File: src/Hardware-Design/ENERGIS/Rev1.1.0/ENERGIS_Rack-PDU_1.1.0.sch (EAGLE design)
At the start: 423 parts, among them IC1 MP2315GJ-Z, IC10 HLW8032, IC11 HLW8032, IC12 HLW8032, IC13 MP150GJ, IC14 HLW8032, IC15 RP2040, IC16 HLW8032, IC17 MCP6001RT-I/OT, IC18 W25Q128JVPIQ, IC19 CAT24C256HU4IGT3, IC2 MP2315GJ-Z, IC20 W5500, IC21 MIC5504-3.3YM5, IC22 MCP6001RT-I/OT, IC3 ULN2803AFWG, IC4 MCP23017T-E/ML, IC5 MP150GJ, IC6 HLW8032, IC7 HLW8032, IC8 HLW8032, IC9 SN74HC151PWR, J10 0R 1%, J2 JP, J7 JP, J8 0R 1%, J9 0R 1%, K1 G2RL-1A-E DC12, K2 G2RL-1A-E DC12, K3 G2RL-1A-E DC12, K4 G2RL-1A-E DC12, K5 G2RL-1A-E DC12, K6 G2RL-1A-E DC12, K7 G2RL-1A-E DC12, K8 G2RL-1A-E DC12, P12ON Green, P3ON Green, P5ON Green, SW3 TP, X1 ABM8-272-T3 12MHz, X2 25MHz

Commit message: add pcap tests. Small fixes
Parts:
- removed FB-NI1, FB-NI2, VNI1, VNI2: TP, ds_passive:TP
- removed GDGC: (no value), ds_con:CON-1X4
- added ADC12, FB1, FB2, VCC, VCC2: TP-ROUND, ds_passive:TP-ROUND
- added GDRC: (no value), ds_con:CON-1X4
- 12VDC, 5V-NI1, 5V-NI2, L-REC1, L-REC2, REL0, REL1, REL2, REL3, REL4, REL5, REL6, REL7, RX0, RX1, SCL0, SCL1, SDA0, SDA1: value TP -> TP-ROUND; device ds_passive:TP -> ds_passive:TP-ROUND
- R17, R18, R19, R20, R21, R22, R23, R24: value 330R 1% 1W -> 0R 1%; device ds_resistor:330R-1%-2512 -> ds_resistor:0R2512
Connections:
- net +12V_MEA: now also ADC12.P$1
- net FB1: now also FB1.P$1; no longer FB-NI1.P$1
- net FB2: now also FB2.P$1; no longer FB-NI2.P$1
- net GND: now also GDRC.P$4; no longer GDGC.P$4
- net RUN: now also GDRC.P$2; no longer GDGC.P$2
- net SWCLK: now also GDRC.P$1; no longer GDGC.P$1
- net SWDIO: now also GDRC.P$3; no longer GDGC.P$3
- net VNI1: now also VCC.P$1; no longer VNI1.P$1
- net VNI2: now also VCC2.P$1; no longer VNI2.P$1
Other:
- note added: "12VDC"
- note added: "230VAC"
- note added: "5V NON-ISOLATED"
- note added: "DEBUG CONNECTOR"
- note added: "Design Note — 12 V supply (Mean Well IRM-10 series), universal 110 V/230 V AC This schematic uses the Mean Well IRM-10 encapsulated AC-DC module (e.g., IRM-10-12) to produce 12 VDC. The IRM-10 series is specified for a wide input range of 85–305 VAC (47–440 Hz) and 120–430 VDC, meaning it operates from both ~115 VAC and ~230 VAC mains with no selector or changes to the circuit. Safety approvals (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"
- note added: "Design Note — 5 V / 200 mA non-isolated supply (MP150), universal 110 V/230 V AC This design uses MPS MP150 in high-side buck to generate 5 V/200 mA directly from rectified mains. MP150 integrates a 500 V MOSFET (Drain-to-Source rating 500 V), covering the ~325 VDC peak from 230 VAC and ~155 VDC from 115 VAC, so the circuit from 85–265 VAC (“universal input”)."
- note added: "ENABLE/DISABLE"
- note added: "FAN CONNECTOR"
- note added: "MCU"
- note added: "PERIPHERALS"
- note added: "USB-C 5VDC"
- note removed: "5V AC-MEASUREMENT"
- note removed: "DEBUG"
- note removed: "FAN"
- note removed: "Rev 1.0.1"

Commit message: adapt design to NextPCB dru
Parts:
- removed CS0, MISO0, MOSI0, SCLK0: TP, ds_passive:TP
- added CS, MI, MO, SC: TP-ROUND, ds_passive:TP-ROUND
- added R166, R167, R168: 3.3K 1%, ds_resistor:3.3K-1%0402
- 3VDC, 3VFB, 5VDC, 5VFB, AVDD, CS1, DVDD, GND, GND-3, GND-5, IOVDD, MISO1, MOSI1, SCLK1, SW, SW3, VBUS, VREF: value TP -> TP-ROUND; device ds_passive:TP -> ds_passive:TP-ROUND
- R130: device ds_resistor:3.3K-1%_ARRAY0603X4-1206 -> ds_resistor:3.3K-1%0402
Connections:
- net +3V3_MCU: now also R130.1, R166.1, R167.1, R168.1; no longer R130.5, R130.6, R130.7, R130.8
- net I2C0_SCL: now also R130.2; no longer R130.1
- net I2C0_SDA: now also R166.2; no longer R130.2
- net I2C1_SCL: now also D18.2, R167.2; no longer D18.1, R130.3
- net I2C1_SDA: now also D18.1, R168.2; no longer D18.2, R130.4
- net LCD_CS: now also CS.P$1; no longer CS0.P$1
- net LCD_MISO: now also MI.P$1; no longer MISO0.P$1
- net LCD_MOSI: now also MO.P$1; no longer MOSI0.P$1
- net LCD_SCLK: now also SC.P$1; no longer SCLK0.P$1

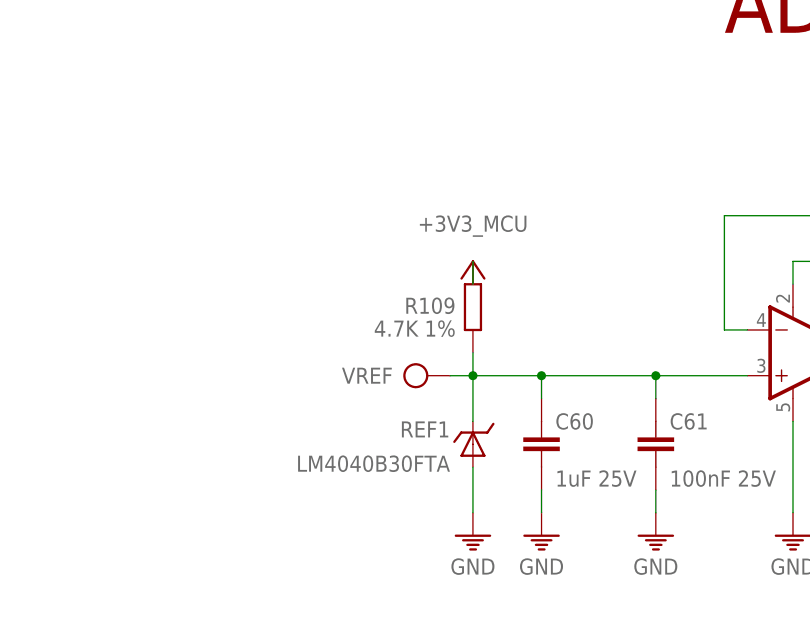
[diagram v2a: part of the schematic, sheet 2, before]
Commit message: update component library to NextPCB
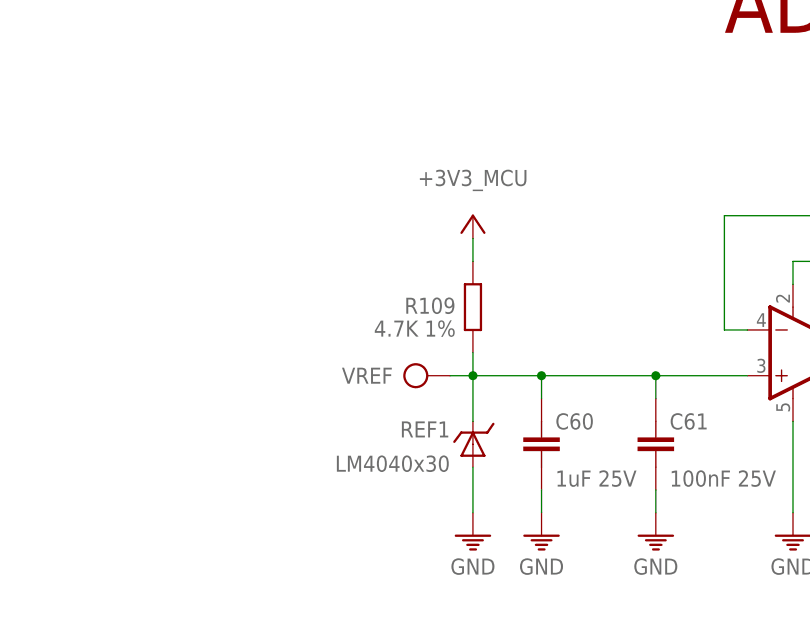
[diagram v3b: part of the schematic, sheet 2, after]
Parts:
- 12VDC, 3VDC, 3VFB, 5V-NI1, 5V-NI2, 5VDC, 5VFB, ADC12, AVDD, CS, CS1, DVDD, FB1, FB2, GND, GND-3, GND-5, IOVDD, L-REC1, L-REC2, MI, MISO1, MO, MOSI1, REL0, REL1, REL2, REL3, REL4, REL5, REL6, REL7, RX0, RX1, SC, SCL0, SCL1, SCLK1, SDA0, SDA1, SW, SW3, VBUS, VCC, VCC2, VREF: value TP-ROUND -> TESTPOINT
- IC9: value SN74HC151PWR -> CD74ACT151M96; device ds_ic_logic:SN74HC151PWR -> ds_ic_logic:74AC151
- REF1: value LM4040B30FTA -> LM4040x30

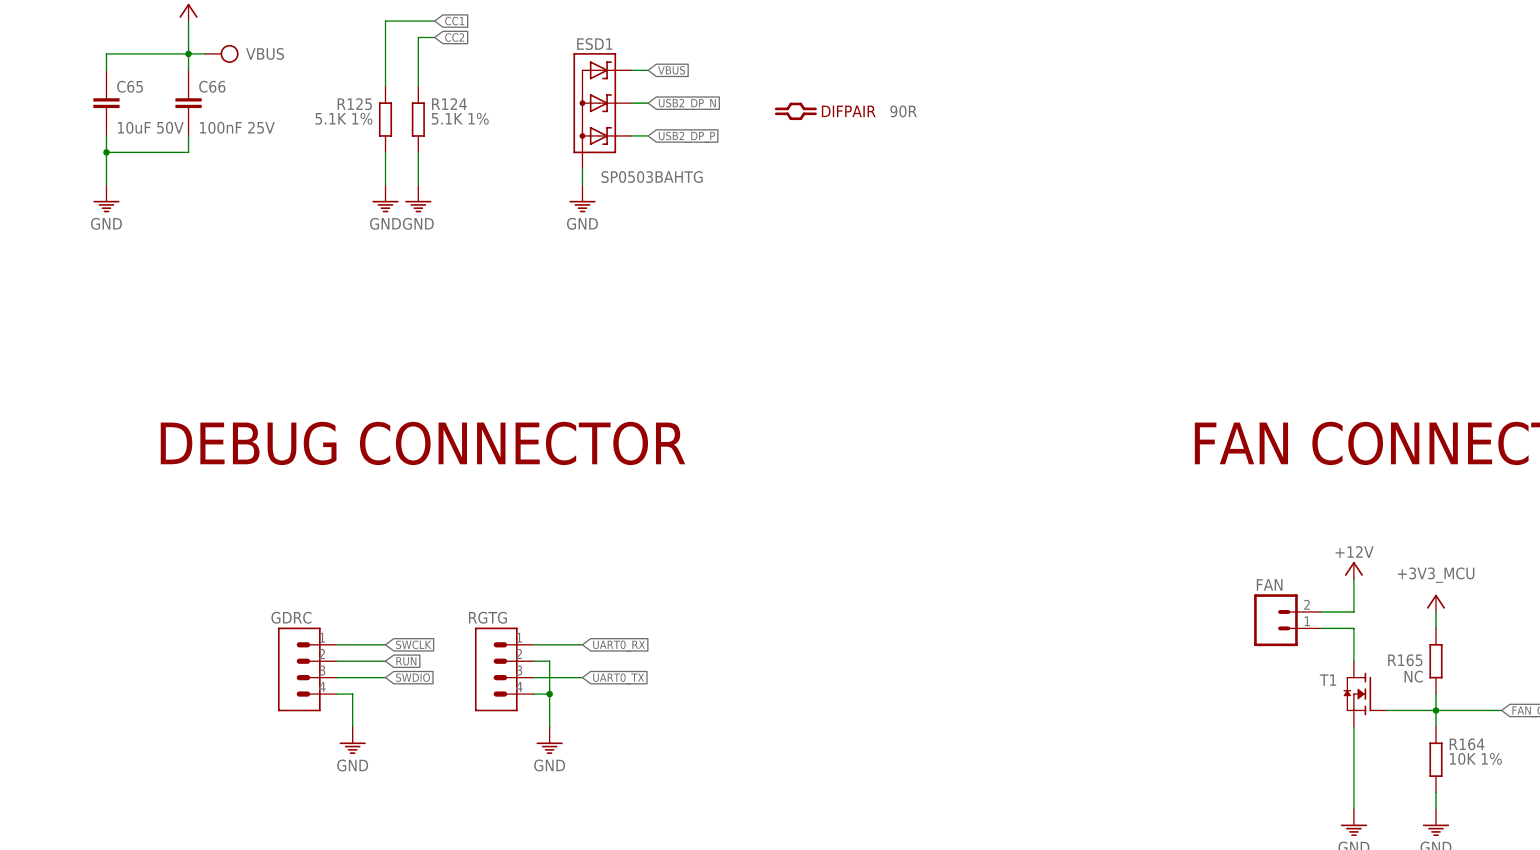
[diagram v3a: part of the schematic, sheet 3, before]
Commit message: update component library to NextPCB
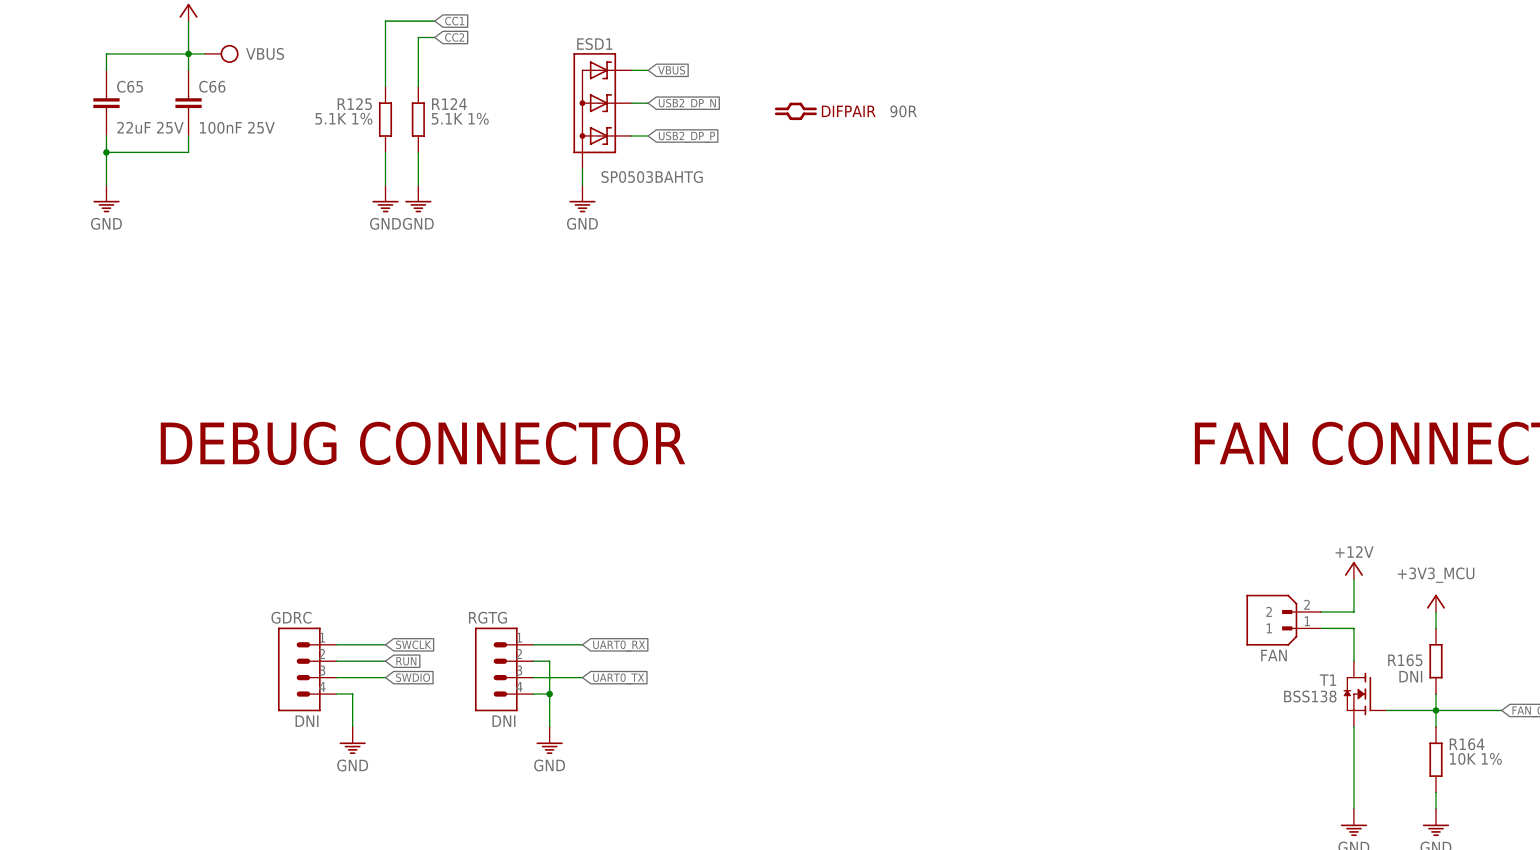
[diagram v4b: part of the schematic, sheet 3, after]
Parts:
- AC/DC2: value IRM-10-15 -> DNI
- AC_L, AC_N: value MOUNT-PAD-ROUND3.0 -> DNI
- C35, C47: value 2.2uF 400V -> 2.2uF 400v; device ds_capacitors:2.2UF-400V6.3X7.7(DXL) -> ds_capacitors:2.2UF-400V6.3X10.5(DXL)
- C65, C97, C99: value 10uF 50V -> 22uF 25V; device ds_capacitors:10UF-50V-0805 -> ds_capacitors:22UF-25V-0805
- C83: device ds_passive:C-1206 -> ds_capacitors:1NF-2KV
- FAN: device con-amp-quick:M02 -> ds_con:JST-B2B-XH-A
- GDRC, RGTG: value (none) -> DNI
- J2, J7: value JP -> DNI
- L1: value 4.9uH -> 4.7uH; device ds_passive:L -> ds_inductor:4.7UH
- L2: value 4.2uH -> 4.7uH; device ds_passive:L -> ds_inductor:4.7UH
- L_OUT1, L_OUT2, L_OUT3, L_OUT4, L_OUT5, L_OUT6, L_OUT7, L_OUT8, N_OUT1, N_OUT2, N_OUT3, N_OUT4, N_OUT5, N_OUT6, N_OUT7, N_OUT8: value MOUNT-PAD-ROUND2.8 -> DNI
- R10: value 33K -> 33K 1%; device ds_passive:R0402 -> ds_resistor:33K-1%0402
- R128, R165: value NC -> DNI
- R143: device ds_passive:R0201 -> ds_resistor:12.4K-1%0201
- T1: value (none) -> BSS138

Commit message: update Readme
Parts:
- D17, D18: device ds_diode:RCLAMP0582BQTCT -> ds_diode:RCLAMP0582BQTCT-

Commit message: update Gerbers
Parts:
- added J1: DNI, Wurth_Connectors_WR-FSH:696101000002
- 12VDC, 3VDC, 3VFB, 5V-NI1, 5V-NI2, 5VDC, 5VFB, ADC12, AVDD, CS, CS1, DVDD, FB1, FB2, GND, GND-3, GND-5, IOVDD, L-REC1, L-REC2, MI, MISO1, MO, MOSI1, REL0, REL1, REL2, REL3, REL4, REL5, REL6, REL7, RX0, RX1, SC, SCL0, SCL1, SCLK1, SDA0, SDA1, SW, SW3, VBUS, VCC, VCC2, VREF: value TESTPOINT -> DNI
- K1, K2, K3, K4, K5, K6, K7, K8: value G2RL-1A-E DC12 -> G2RL-1A-E_DC12
- X1: value ABM8-272-T3 12MHz -> 12MHz
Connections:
- new net AC_L_F: AC_L.MOUNT, J1.1
- net AC_L: now also J1.2; no longer AC_L.MOUNT
